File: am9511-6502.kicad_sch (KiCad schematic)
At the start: 14 parts, among them J1 Conn_01x18_Pin, U1 AM9511A, U2 GAL16V8, U3 74HC112, U4 ADA-TPS61040, U5 74HC123, X1 4 MHz

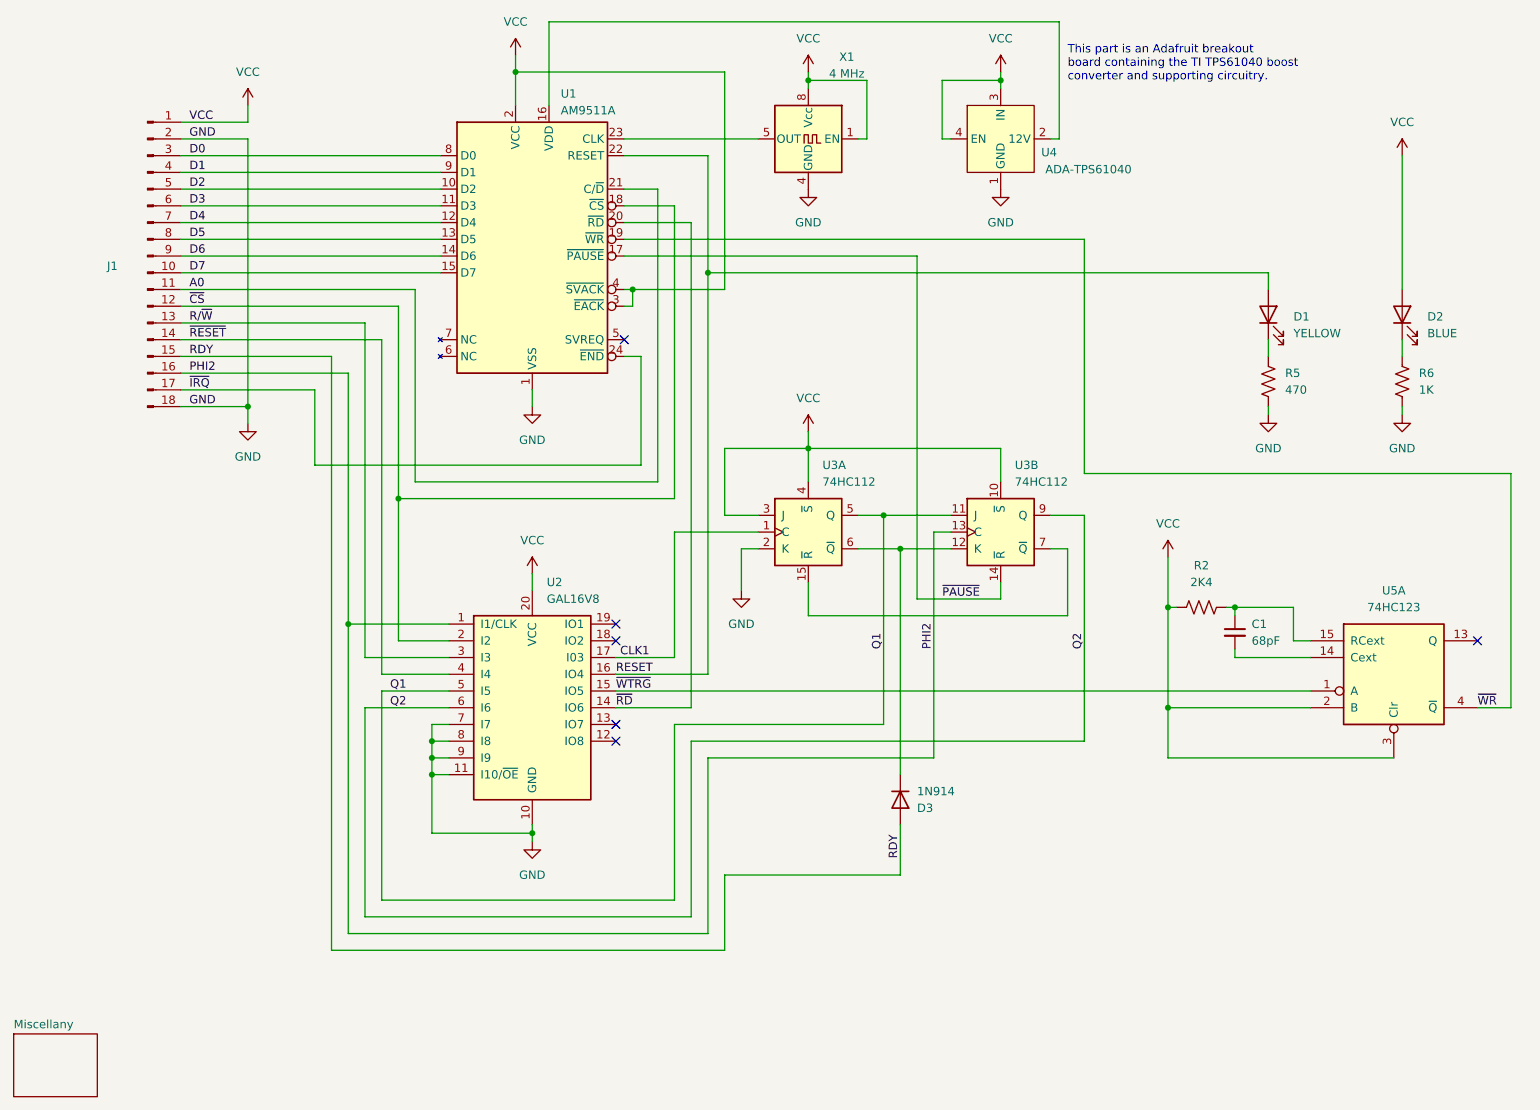
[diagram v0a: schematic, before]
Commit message: move custom symbols and footprints to project libraries
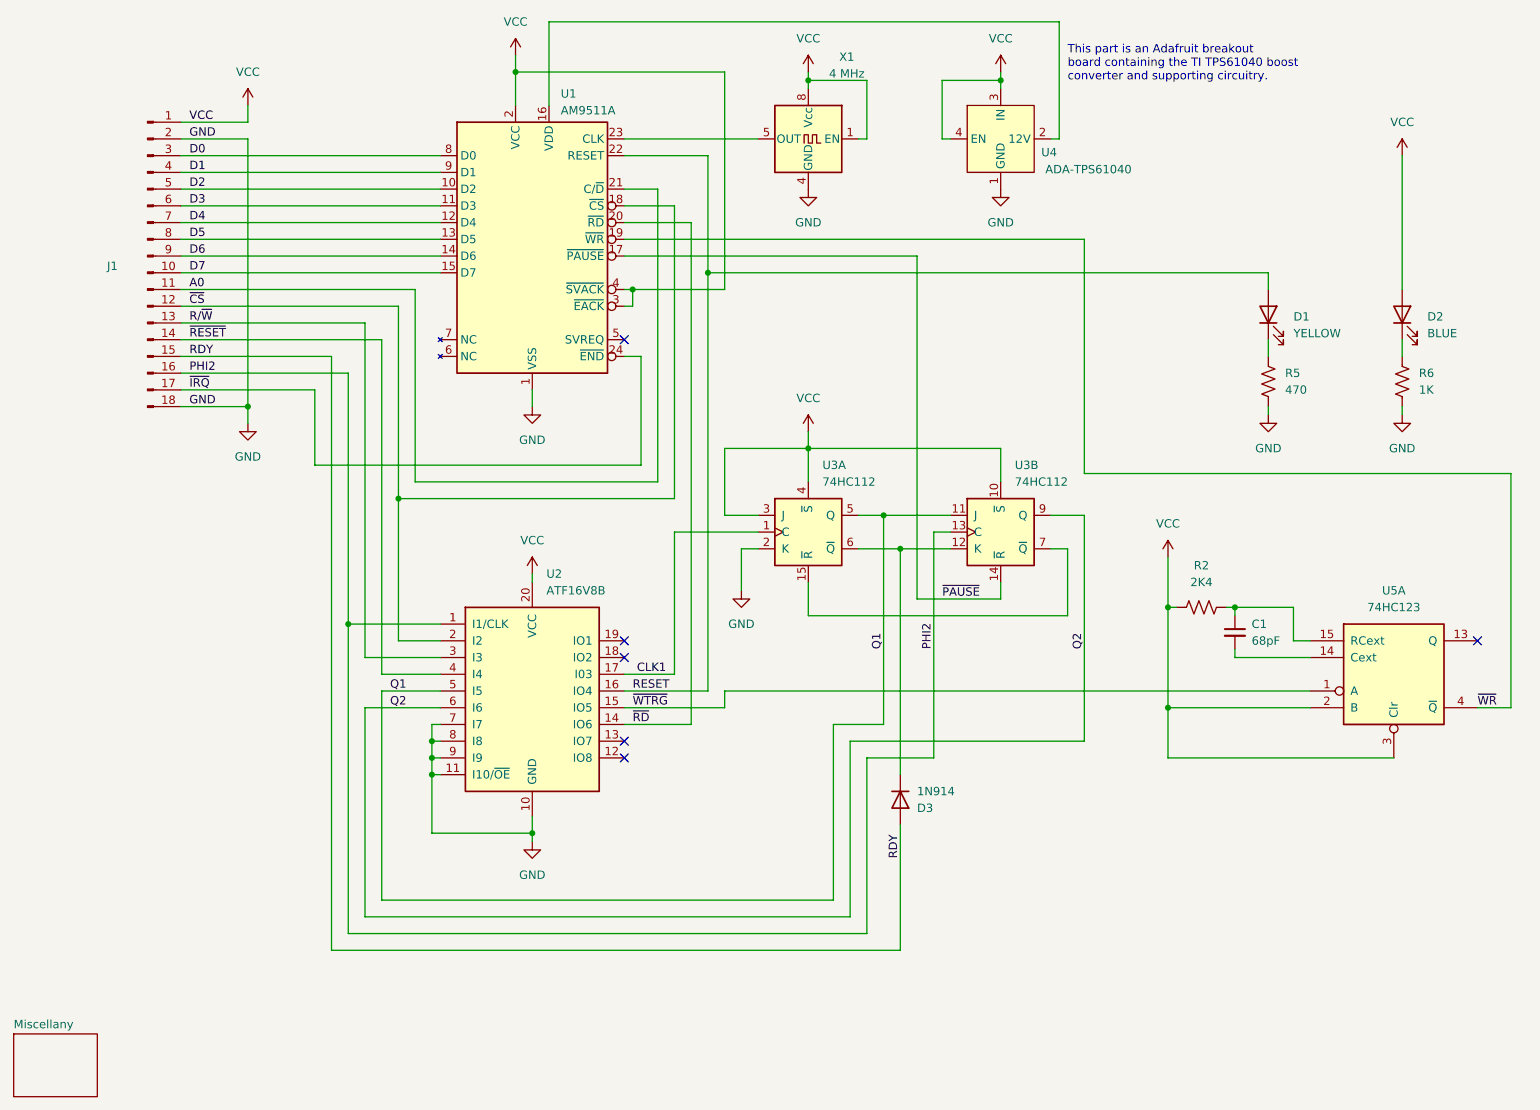
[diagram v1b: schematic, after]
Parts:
- U1: symbol local:AM9511 -> am9511-6502-symbols:AM9511
- U2: value GAL16V8 -> ATF16V8B; symbol Logic_Programmable:GAL16V8 -> am9511-6502-symbols:ATF16V8B
- U3: symbol local:74HC112 -> am9511-6502-symbols:74HC112
- U4: symbol local:ADA-TPS61040 -> am9511-6502-symbols:ADA-TPS61040
- U5: symbol 74xx:74HC123 -> am9511-6502-symbols:74HC123
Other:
- title: AM9511 Interface for 65C09 -> AM9511 Interface for 6509
- moved on the sheet: U2
